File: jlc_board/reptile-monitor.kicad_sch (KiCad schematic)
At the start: 32 parts, among them J1 AudioJack4_SwitchR1, J2 AudioJack4_SwitchR1, J3 PWR CONN, J4 UART, J6 18-Lead FPC 0.5 mm - Vertical, Q1 2SC1741, SW1 RESET, U1 AP2112M-3.3, U2 TCA4307DGKR

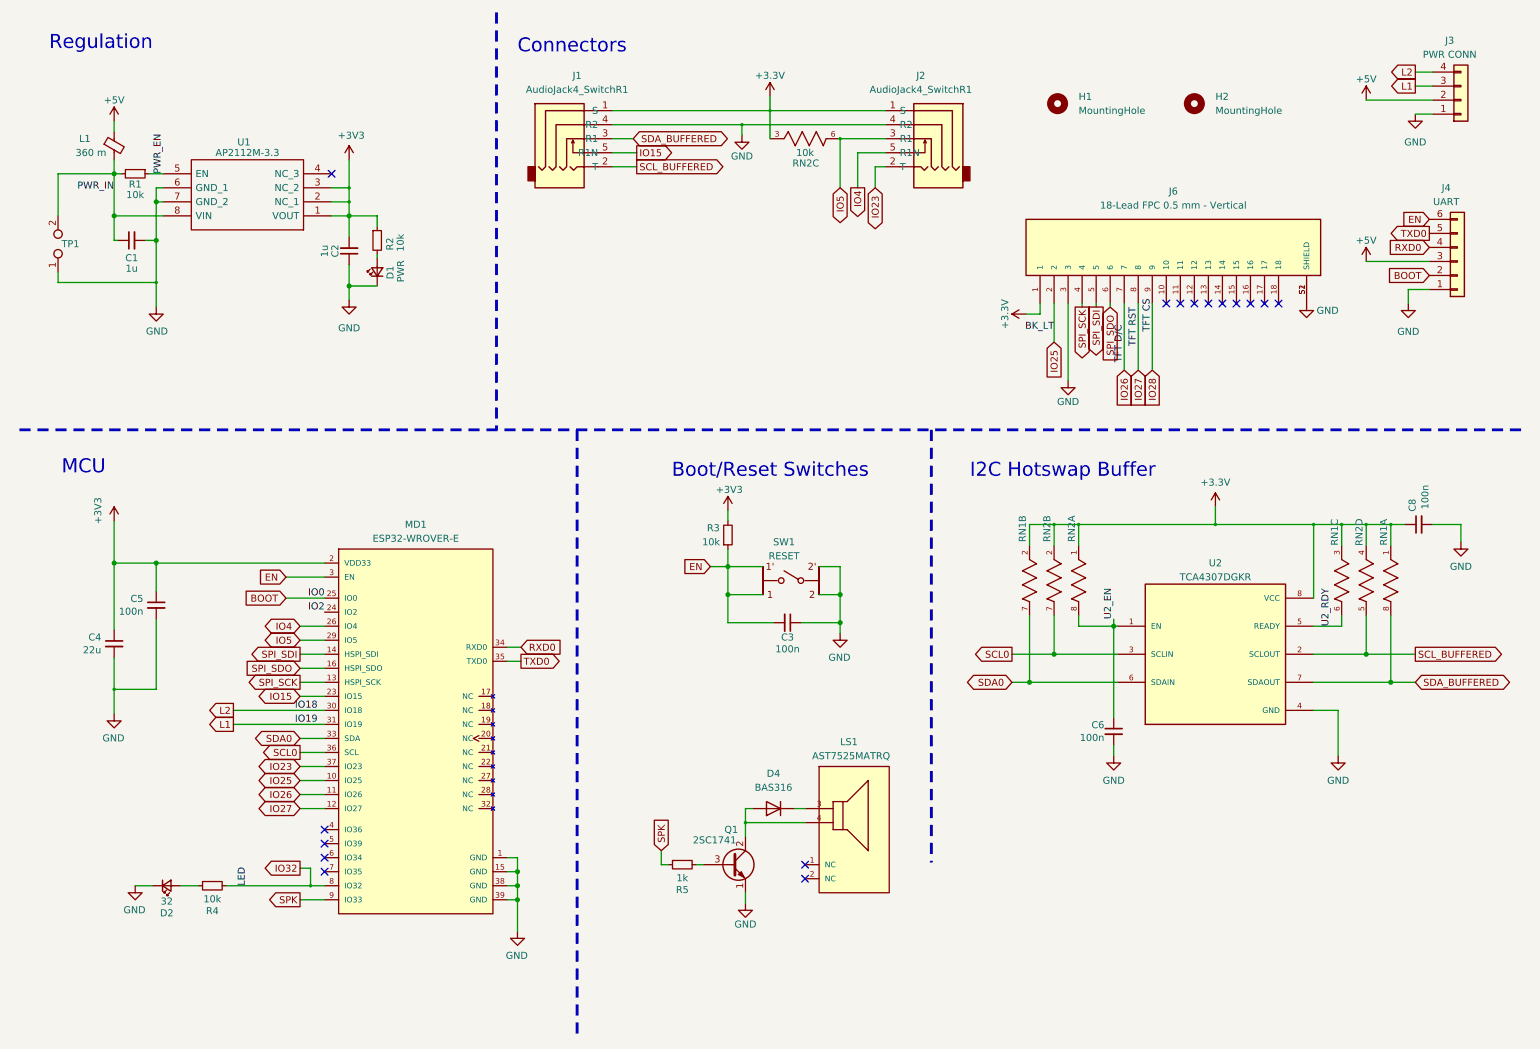
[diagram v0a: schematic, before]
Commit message: Eliminate I2C Chip & move stemma qt connector to top
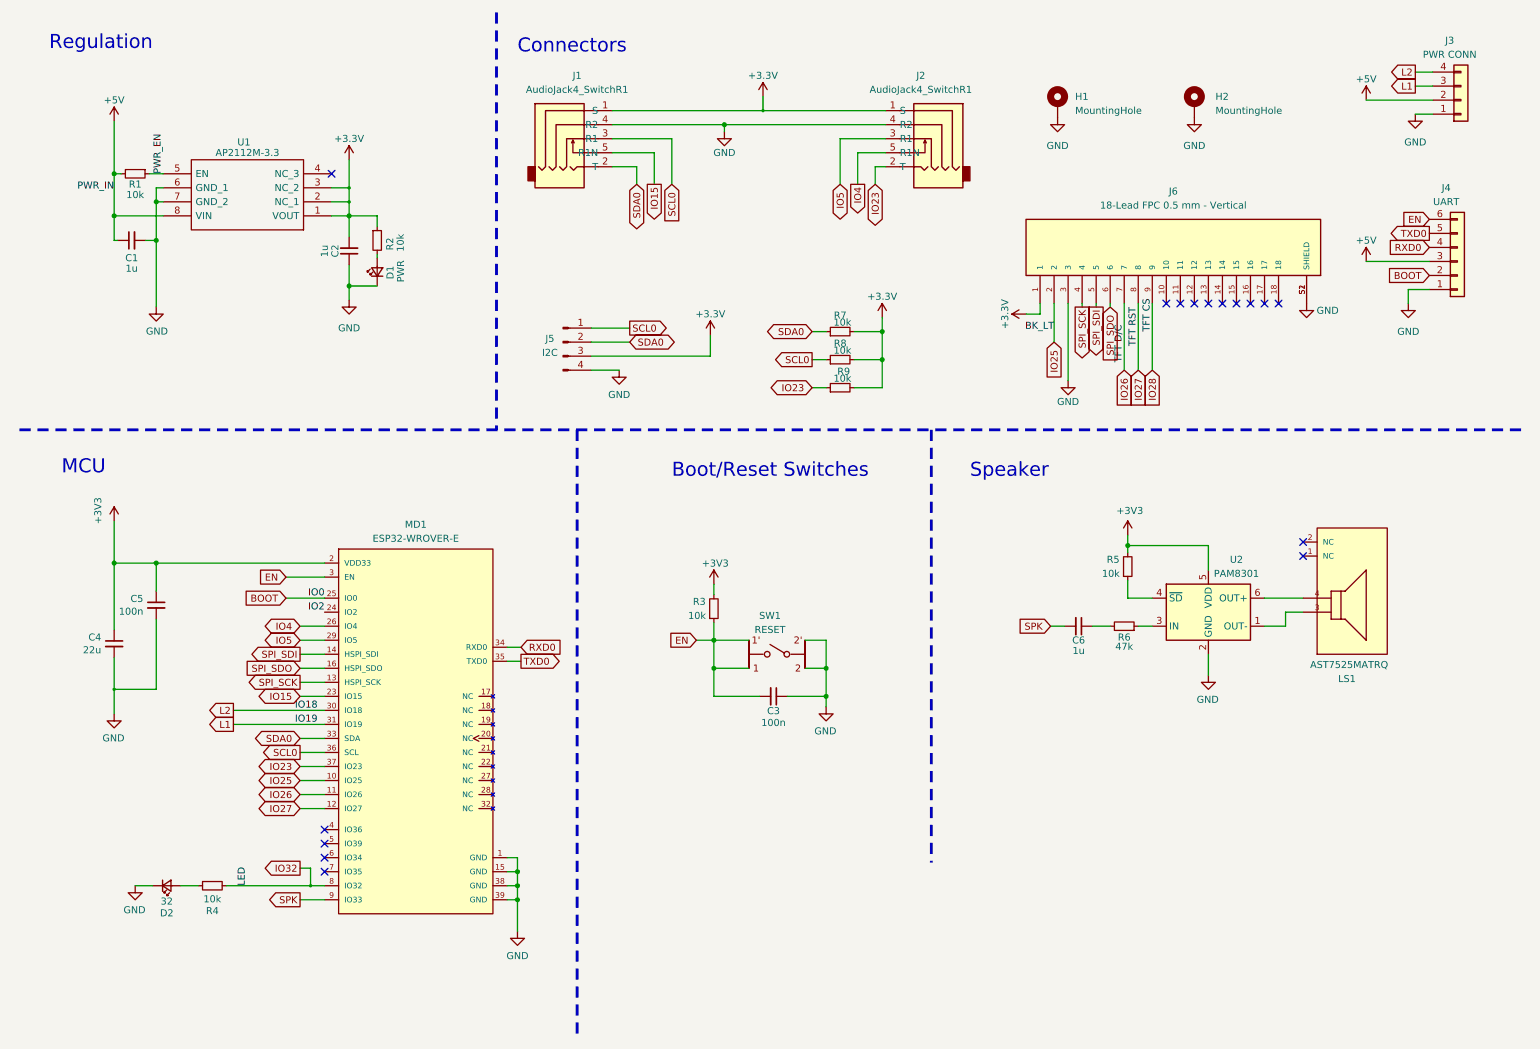
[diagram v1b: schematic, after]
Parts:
- removed C8: 100n, reptile-monitor:C_0603_1608Metric, symbol Device:C_Small
- removed D4: BAS316, reptile-monitor:D_SOD-323, symbol Diode:BAS316
- removed L1: 360 m, reptile-monitor:L_0603_1608Metric, symbol Device:FerriteBead_Small
- removed Q1: 2SC1741, Package_TO_SOT_SMD:SOT-23, symbol Transistor_BJT:2SC1815
- removed RN1, RN2: 10k, reptile-monitor:Panasonic-EXB-V8V103JV-0, symbol reptile-monitor:EXB-V8V103JV
- removed TP1: TestPoint_2Pole, Connector_PinHeader_2.54mm:PinHeader_1x02_P2.54mm_Vertical, symbol Connector:TestPoint_2Pole
- removed U2: TCA4307DGKR, reptile-monitor:VSSOP-8_3.0x3.0mm_P0.65mm, symbol reptile-monitor:TCA4307DGKR
- added J5: I2C, reptile-monitor:JST_SH_SM04B-SRSS-TB_1x04-1MP_P1.00mm_Horizontal, symbol Connector:Conn_01x04_Male
- added R6: 47k, reptile-monitor:R_0603_1608Metric, symbol Device:R_Small
- added R7, R8, R9: 10k, reptile-monitor:R_0603_1608Metric, symbol Device:R_Small
- added U2: PAM8301, Package_TO_SOT_SMD:SOT-23-6, symbol Amplifier_Audio:PAM8301
- C6: value 100n -> 1u; LCSC C84419 -> (none); Series (none) -> X7R or X5R
- H1, H2: footprint MountingHole:MountingHole_2.2mm_M2_ISO7380 -> MountingHole:MountingHole_2.2mm_M2_ISO7380_Pad; symbol Mechanical:MountingHole -> Mechanical:MountingHole_Pad
- R5: value 1k -> 10k
- SW1: footprint reptile-monitor:Panasonic-EVQ-P7A01P-0-0-MFG -> reptile-monitor:Panasonic-EVQ-P7A01P
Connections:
- net PWR_IN is gone; now on net +5V: C1.1, R1.2, U1.8 (VIN)
- net SCL_BUFFERED is gone; now on net SDA0: J1.2 (T)
- net SDA_BUFFERED is gone; now on net SCL0: J1.3 (R1)
- net +3V3: now also R5.2, J5.3 (Pin_3), R7.2, R8.2, R9.2, U2.5 (VDD)
- net GND: now also H1.1, H2.1, J5.4 (Pin_4), U2.2 (GND); no longer C6.2
- net IO23: now also R9.1
- net SCL0: now also J5.1 (Pin_1), R8.1
- net SDA0: now also J5.2 (Pin_2), R7.1
- net SPK: now also C6.2; no longer R5.1
- net at LS1.4 (CATHODE): now also U2.6 (OUT+)
- net at LS1.3 (ANODE): now also U2.1 (OUT-)
- net U2_EN: no longer names the net of C6.1
- net U2_EN: now also R6.2
- new net: R6.1, U2.3 (IN)
- new net: R5.1, U2.4 (~{SD})
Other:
- note added: "Speaker"
- note removed: "I2C Hotswap Buffer"
- moved on the sheet: C3, R3, SW1

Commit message: rev5
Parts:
- removed C6: 1u, reptile-monitor:C_0603_1608Metric, symbol Device:C_Small
- removed D2: 32, reptile-monitor:LED_0603_1608Metric, symbol Device:LED_Small
- removed J5: I2C, reptile-monitor:JST_SH_SM04B-SRSS-TB_1x04-1MP_P1.00mm_Horizontal, symbol Connector:Conn_01x04_Male
- removed R4, R5, R7, R8, R9: 10k, reptile-monitor:R_0603_1608Metric, symbol Device:R_Small
- removed R6: 47k, reptile-monitor:R_0603_1608Metric, symbol Device:R_Small
- removed U2: PAM8301, Package_TO_SOT_SMD:SOT-23-6, symbol Amplifier_Audio:PAM8301
- added D2: WS2812B, reptile-monitor:LED_WS2812B_PLCC4_5.0x5.0mm_P3.2mm, symbol LED:WS2812B
- added D3, D4, D5: 1N4007, reptile-monitor:D_SOD-323, symbol Diode:1N4007
- added Q1: Q_NPN_BEC, reptile-monitor:SOT-23, symbol Device:Q_NPN_BEC
- added R5: 1K, reptile-monitor:R_0603_1608Metric, symbol Device:R
- added RN1: 10k, reptile-monitor:Panasonic-EXB-V8V103JV-0, symbol reptile-monitor:R_Pack04
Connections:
- net IO2 is gone; now on net SD_CS: MD1.24 (IO2)
- net +3V3: now also D2.1 (VDD), RN1.1 (R1.1), RN1.2 (R2.1), RN1.3 (R3.1), RN1.4 (R4.1); no longer U1.2 (NC_1), U1.3 (NC_2)
- net +5V: now also D4.1 (K), D5.1 (K); no longer J3.2 (Pin_2), J4.3 (Pin_3)
- net GND: now also D2.3 (VSS), Q1.2 (E)
- net SCL0: now also J2.3 (R1), RN1.7 (R2.2); no longer J1.3 (R1)
- net SDA0: now also J2.2 (T), RN1.8 (R1.2); no longer J1.2 (T)
- net VDD: now reaches LS1.3 (ANODE)
- net VDD: now also D3.1 (K)
- net at LS1.4 (CATHODE): now also D3.2 (A), Q1.3 (C)
- net SD_CS: now reaches J6.10
- net IO15: no longer names the net of J1.5 (R1N)
- net IO15: no longer MD1.23 (IO15)
- net IO23 renamed DS_0
- net DS_0: now also J1.3 (R1), RN1.6 (R3.2); no longer J2.2 (T)
- net IO25 renamed BK_LT
- net IO26 renamed TFT_DC
- net IO27 renamed TFT_RST
- net IO28 renamed TFT_CS
- net TFT_CS: now also MD1.23 (IO15)
- net IO32 renamed LED
- net LED: now also D2.4 (DIN)
- net IO4: no longer names the net of J2.5 (R1N)
- net IO4: no longer MD1.26 (IO4)
- net IO5: no longer names the net of MD1.29 (IO5)
- net IO5: no longer J2.3 (R1)
- net SPK renamed BUZZER
- net BUZZER: now also R5.1
- new net: D5.2 (A), J3.2 (Pin_2)
- new net: Q1.1 (B), R5.2
- new net: D4.2 (A), J4.3 (Pin_3)
- new net DS_DATA: J1.2 (T), MD1.26 (IO4), RN1.5 (R4.2)
- no-connect marks 16 -> 19
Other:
- moved on the sheet: C3, J4, R3, SW1

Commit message: tt-relay
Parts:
- added U?: LM1117-3.3, symbol Regulator_Linear:LM1117-3.3
- R5: value 1K -> 1k
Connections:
- net +5V: no longer U1.8 (VIN)
- net GND: no longer U1.6 (GND_1), U1.7 (GND_2)
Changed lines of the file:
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@@
   (junction (at 36.83 111.76) (diameter 0.9144) (color 0 0 0 0)
   )
-  (junction (at 36.83 53.34) (diameter 0.9144) (color 0 0 0 0)
-  )
   (junction (at 71.755 48.895) (diameter 0.9144) (color 0 0 0 0)
   )
-  (junction (at 36.83 46.355) (diameter 0.9144) (color 0 0 0 0)
-  )
   (junction (at 158.115 127) (diameter 0.9144) (color 0 0 0 0)
   )
@@
   )
   (junction (at 139.7 32.385) (diameter 0) (color 0 0 0 0)
-  )
-  (junction (at 29.21 48.895) (diameter 0.9144) (color 0 0 0 0)
   )
   (junction (at 156.21 66.04) (diameter 0) (color 0 0 0 0)
@@
     (stroke (width 0) (type default) (color 0 0 0 0))
   )
-  (wire (pts (xy 36.83 46.355) (xy 36.83 53.34))
-    (stroke (width 0) (type solid) (color 0 0 0 0))
-  )
-  (wire (pts (xy 36.83 43.815) (xy 36.83 46.355))
-    (stroke (width 0) (type solid) (color 0 0 0 0))
-  )
   (wire (pts (xy 36.83 53.34) (xy 36.83 65.405))
     (stroke (width 0) (type solid) (color 0 0 0 0))
@@
     (stroke (width 0) (type solid) (color 0 0 0 0))
   )
-  (wire (pts (xy 36.83 46.355) (xy 38.1 46.355))
-    (stroke (width 0) (type solid) (color 0 0 0 0))
-  )
   (wire (pts (xy 215.265 119.38) (xy 220.345 119.38))
     (stroke (width 0) (type default) (color 0 0 0 0))
@@
   (wire (pts (xy 156.21 63.5) (xy 156.21 66.04))
     (stroke (width 0) (type default) (color 0 0 0 0))
-  )
-  (wire (pts (xy 36.83 43.815) (xy 38.1 43.815))
-    (stroke (width 0) (type solid) (color 0 0 0 0))
   )
   (wire (pts (xy 227.965 113.03) (xy 227.965 114.3))
@@
     (stroke (width 0) (type default) (color 0 0 0 0))
   )
-  (wire (pts (xy 29.21 41.275) (xy 29.21 48.895))
+  (wire (pts (xy 29.21 41.275) (xy 29.21 53.34))
     (stroke (width 0) (type solid) (color 0 0 0 0))
   )
@@
     (stroke (width 0) (type solid) (color 0 0 0 0))
   )
-  (wire (pts (xy 29.21 48.895) (xy 29.21 53.34))
-    (stroke (width 0) (type solid) (color 0 0 0 0))
-  )
   (wire (pts (xy 102.87 129.54) (xy 100.33 129.54))
     (stroke (width 0) (type solid) (color 0 0 0 0))
@@
   (wire (pts (xy 138.43 66.04) (xy 140.97 66.04))
     (stroke (width 0) (type default) (color 0 0 0 0))
-  )
-  (wire (pts (xy 29.21 48.895) (xy 38.1 48.895))
-    (stroke (width 0) (type solid) (color 0 0 0 0))
   )
   (wire (pts (xy 119.38 40.005) (xy 124.46 40.005))
@@
     (pin "4" (alternate "-"))
   )
-  (symbol (lib_id "power:+3.3V") (at 156.21 63.5 0) (mirror y) (unit 1)
-    (in_bom yes) (on_board yes)
-    (property "Reference" "#PWR013" (id 0) (at 156.21 67.31 0)
-      (effects (font (size 1.27 1.27)) hide)
-    )
-    (property "Value" "+3.3V" (id 1) (at 156.21 59.69 0))
-    (property "Footprint" "" (id 2) (at 156.21 63.5 0)
-      (effects (font (size 1.27 1.27)) hide)
-    )
-    (property "Datasheet" "" (id 3) (at 156.21 63.5 0)
-      (effects (font (size 1.27 1.27)) hide)
-    )
-    (pin "1")
-  )
-  (symbol (lib_id "power:+3.3V") (at 146.685 27.305 0) (unit 1)
-    (in_bom yes) (on_board yes)
-    (property "Reference" "#PWR020" (id 0) (at 146.685 31.115 0)
-      (effects (font (size 1.27 1.27)) hide)
-    )
-    (property "Value" "+3.3V" (id 1) (at 146.685 23.495 0))
-    (property "Footprint" "" (id 2) (at 146.685 27.305 0)
-      (effects (font (size 1.27 1.27)) hide)
-    )
-    (property "Datasheet" "" (id 3) (at 146.685 27.305 0)
+  (symbol (lib_id "power1:+3V3") (at 71.755 38.735 0) (mirror y) (unit 1)
+    (in_bom yes) (on_board yes)
+    (property "Reference" "#PWR?" (id 0) (at 71.755 42.545 0)
+      (effects (font (size 1.27 1.27)) hide)
+    )
+    (property "Value" "+3V3" (id 1) (at 72.009 34.9758 0))
+    (property "Footprint" "" (id 2) (at 71.755 38.735 0)
+      (effects (font (size 1.27 1.27)) hide)
+    )
+    (property "Datasheet" "" (id 3) (at 71.755 38.735 0)
       (effects (font (size 1.27 1.27)) hide)
     )
@@
     (pin "2'")
   )
+  (symbol (lib_id "Regulator_Linear:LM1117-3.3") (at 53.34 57.15 0) (unit 1)
+    (in_bom yes) (on_board yes) (fields_autoplaced)
+    (property "Reference" "U?" (id 0) (at 53.34 49.53 0))
+    (property "Value" "LM1117-3.3" (id 1) (at 53.34 52.07 0))
+    (property "Footprint" "" (id 2) (at 53.34 57.15 0)
+      (effects (font (size 1.27 1.27)) hide)
+    )
+    (property "Datasheet" "http://www.ti.com/lit/ds/symlink/lm1117.pdf" (id 3) (at 53.34 57.15 0)
+      (effects (font (size 1.27 1.27)) hide)
+    )
+    (pin "1")
+    (pin "2")
+    (pin "3")
+  )
   (symbol (lib_id "power:GND") (at 227.965 127.635 0) (unit 1)
     (in_bom yes) (on_board yes) (fields_autoplaced)
@@
     (pin "1")
   )
+  (symbol (lib_id "power1:+3V3") (at 146.685 27.305 0) (mirror y) (unit 1)
+    (in_bom yes) (on_board yes)
+    (property "Reference" "#PWR?" (id 0) (at 146.685 31.115 0)
+      (effects (font (size 1.27 1.27)) hide)
+    )
+    (property "Value" "+3V3" (id 1) (at 146.939 23.5458 0))
+    (property "Footprint" "" (id 2) (at 146.685 27.305 0)
+      (effects (font (size 1.27 1.27)) hide)
+    )
+    (property "Datasheet" "" (id 3) (at 146.685 27.305 0)
+      (effects (font (size 1.27 1.27)) hide)
+    )
+    (pin "1")
+  )
   (symbol (lib_id "power1:GND") (at 224.79 31.115 0) (mirror y) (unit 1)
     (in_bom yes) (on_board yes) (fields_autoplaced)
@@
     (pin "1")
     (pin "2")
-  )
-  (symbol (lib_id "power1:+3.3V") (at 71.755 38.735 0) (unit 1)
-    (in_bom yes) (on_board yes)
-    (property "Reference" "#PWR0108" (id 0) (at 71.755 42.545 0)
-      (effects (font (size 1.27 1.27)) hide)
-    )
-    (property "Value" "+3.3V" (id 1) (at 71.755 34.925 0))
-    (property "Footprint" "" (id 2) (at 71.755 38.735 0)
-      (effects (font (size 1.27 1.27)) hide)
-    )
-    (property "Datasheet" "" (id 3) (at 71.755 38.735 0)
-      (effects (font (size 1.27 1.27)) hide)
-    )
-    (pin "1" (alternate "+3V3-OUT"))
   )
   (symbol (lib_id "Device:LED_Small") (at 76.835 59.055 90) (unit 1)
@@
     (in_bom yes) (on_board yes)
     (property "Reference" "R5" (id 0) (at 211.455 114.935 90))
-    (property "Value" "1K" (id 1) (at 211.455 116.84 90))
+    (property "Value" "1k" (id 1) (at 211.455 116.84 90))
     (property "Footprint" "reptile-monitor:R_0603_1608Metric" (id 2) (at 211.455 121.158 90)
       (effects (font (size 1.27 1.27)) hide)
@@
     )
     (property "Datasheet" "" (id 3) (at 245.11 64.77 0)
+      (effects (font (size 1.27 1.27)) hide)
+    )
+    (pin "1")
+  )
+  (symbol (lib_id "power1:+3V3") (at 156.21 63.5 0) (mirror y) (unit 1)
+    (in_bom yes) (on_board yes)
+    (property "Reference" "#PWR?" (id 0) (at 156.21 67.31 0)
+      (effects (font (size 1.27 1.27)) hide)
+    )
+    (property "Value" "+3V3" (id 1) (at 156.464 59.7408 0))
+    (property "Footprint" "" (id 2) (at 156.21 63.5 0)
+      (effects (font (size 1.27 1.27)) hide)
+    )
+    (property "Datasheet" "" (id 3) (at 156.21 63.5 0)
       (effects (font (size 1.27 1.27)) hide)
     )
@@
       (reference "#PWR011") (unit 1) (value "GND") (footprint "")
     )
-    (path "/348c3b2c-dd62-4215-9736-618c0f2f443f"
-      (reference "#PWR013") (unit 1) (value "+3.3V") (footprint "")
-    )
     (path "/996ef5ef-126b-4068-807b-3db412b745bb"
       (reference "#PWR015") (unit 1) (value "+3V3") (footprint "")
@@
       (reference "#PWR018") (unit 1) (value "GND") (footprint "")
     )
-    (path "/3f5eff73-a3d5-4baa-ad32-6a06b984b9fe"
-      (reference "#PWR020") (unit 1) (value "+3.3V") (footprint "")
-    )
     (path "/99e75a67-11d8-4315-8161-3841454f4971"
       (reference "#PWR0101") (unit 1) (value "GND") (footprint "")
@@
       (reference "#PWR0107") (unit 1) (value "GND") (footprint "")
     )
-    (path "/8d96b1db-19d6-45b2-b8e5-eee9973e5e45"
-      (reference "#PWR0108") (unit 1) (value "+3.3V") (footprint "")
-    )
     (path "/c8a1977b-1088-4796-a512-3034692ac264"
       (reference "#PWR0109") (unit 1) (value "VDD") (footprint "")
     )
+    (path "/3919b715-f4d5-4cea-b04f-b47e2701b39e"
+      (reference "#PWR?") (unit 1) (value "+3V3") (footprint "")
+    )
+    (path "/85464d22-8278-4e21-8ac5-8c99a20e3b98"
+      (reference "#PWR?") (unit 1) (value "+3V3") (footprint "")
+    )
+    (path "/e3a9f70e-1533-45c2-b13e-a8accbd27639"
+      (reference "#PWR?") (unit 1) (value "+3V3") (footprint "")
+    )
     (path "/0583779a-839b-42e1-9b54-47d3c2ffaf32"
       (reference "C1") (unit 1) (value "1u") (footprint "reptile-monitor:C_0603_1608Metric")
@@
     )
     (path "/c0973278-5da1-4770-8cdb-f615ca47cd6a"
-      (reference "R5") (unit 1) (value "1K") (footprint "reptile-monitor:R_0603_1608Metric")
+      (reference "R5") (unit 1) (value "1k") (footprint "reptile-monitor:R_0603_1608Metric")
     )
     (path "/bfff83f9-274a-4d56-97ee-a4caeb4a694d"
@@
       (reference "U1") (unit 1) (value "AP2112M-3.3") (footprint "reptile-monitor:SOIC127P600X170-8N")
     )
-  )
+    (path "/5d1de36e-0591-465f-a55e-a456bc8d900f"
+      (reference "U?") (unit 1) (value "LM1117-3.3") (footprint "")
+    )
+  )
